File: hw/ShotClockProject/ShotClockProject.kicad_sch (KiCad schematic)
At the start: 8 parts, among them SW1 TK-6580S-1

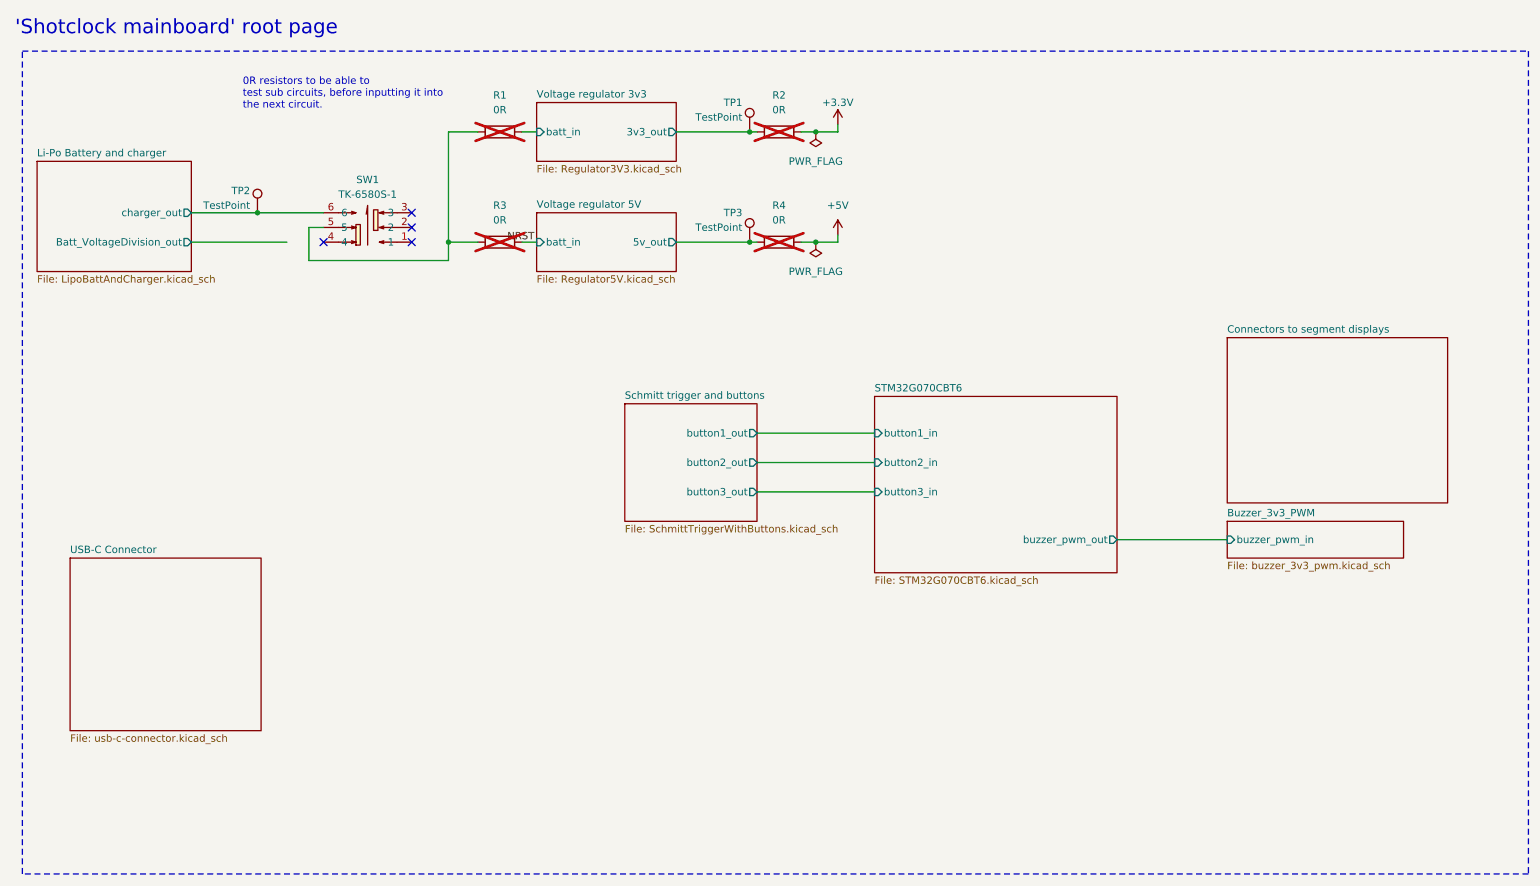
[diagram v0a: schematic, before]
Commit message: Routing on mainboard for LiPo charger
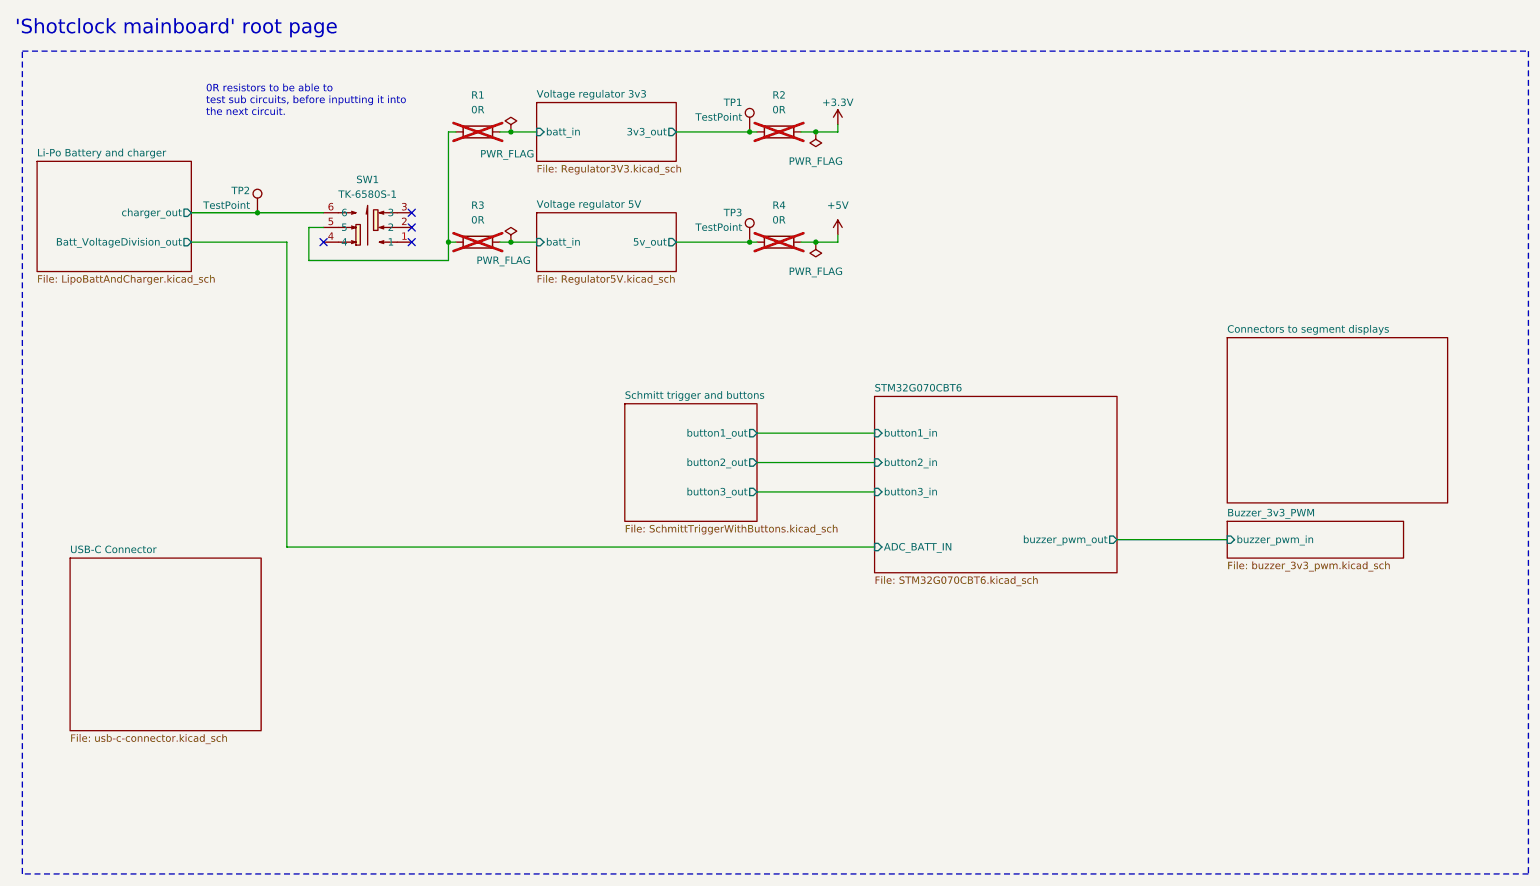
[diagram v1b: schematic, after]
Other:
- sheet STM32G070CBT6 ports: added ADC_BATT_IN; removed none
- moved on the sheet: R1, R3
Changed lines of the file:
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@@
   (junction (at 156.21 54.61) (diameter 0) (color 0 0 0 0)
+  )
+  (junction (at 103.505 54.61) (diameter 0) (color 0 0 0 0)
+  )
+  (junction (at 103.505 35.56) (diameter 0) (color 0 0 0 0)
   )
   (junction (at 59.69 49.53) (diameter 0) (color 0 0 0 0)
@@
     (stroke (width 0) (type default))
   )
+  (wire (pts (xy 103.505 54.61) (xy 107.95 54.61))
+    (stroke (width 0) (type default))
+  )
+  (wire (pts (xy 68.58 57.785) (xy 92.71 57.785))
+    (stroke (width 0) (type default))
+  )
   (wire (pts (xy 208.28 106.045) (xy 227.33 106.045))
     (stroke (width 0) (type default))
@@
     (stroke (width 0) (type default))
   )
+  (wire (pts (xy 92.71 35.56) (xy 92.71 54.61))
+    (stroke (width 0) (type default))
+  )
   (wire (pts (xy 156.21 54.61) (xy 160.02 54.61))
     (stroke (width 0) (type default))
   )
+  (wire (pts (xy 103.505 35.56) (xy 107.95 35.56))
+    (stroke (width 0) (type default))
+  )
   (wire (pts (xy 92.71 57.785) (xy 92.71 54.61))
     (stroke (width 0) (type default))
@@
     (stroke (width 0) (type default))
   )
-  (wire (pts (xy 105.41 35.56) (xy 107.95 35.56))
+  (wire (pts (xy 101.6 35.56) (xy 103.505 35.56))
     (stroke (width 0) (type default))
   )
@@
     (stroke (width 0) (type default))
   )
-  (wire (pts (xy 92.71 54.61) (xy 97.79 54.61))
+  (wire (pts (xy 92.71 54.61) (xy 93.98 54.61))
     (stroke (width 0) (type default))
   )
@@
     (stroke (width 0) (type default))
   )
-  (wire (pts (xy 92.71 35.56) (xy 92.71 54.61))
-    (stroke (width 0) (type default))
-  )
   (wire (pts (xy 160.02 54.61) (xy 160.02 53.34))
     (stroke (width 0) (type default))
   )
-  (wire (pts (xy 68.58 57.785) (xy 92.71 57.785))
-    (stroke (width 0) (type default))
-  )
-  (wire (pts (xy 97.79 35.56) (xy 92.71 35.56))
+  (wire (pts (xy 93.98 35.56) (xy 92.71 35.56))
     (stroke (width 0) (type default))
   )
@@
     (stroke (width 0) (type default))
   )
+  (wire (pts (xy 64.77 54.61) (xy 64.77 107.315))
+    (stroke (width 0) (type default))
+  )
   (wire (pts (xy 160.02 35.56) (xy 160.02 34.29))
     (stroke (width 0) (type default))
@@
     (stroke (width 0) (type default))
   )
-  (wire (pts (xy 105.41 54.61) (xy 107.95 54.61))
+  (wire (pts (xy 101.6 54.61) (xy 103.505 54.61))
     (stroke (width 0) (type default))
   )
   (wire (pts (xy 146.05 97.79) (xy 166.37 97.79))
+    (stroke (width 0) (type default))
+  )
+  (wire (pts (xy 64.77 107.315) (xy 166.37 107.315))
     (stroke (width 0) (type default))
   )
@@
   )
   (text "0R resistors to be able to \ntest sub circuits, before inputting it into\nthe next circuit."
-    (at 57.15 31.75 0)
+    (at 50.8 33.02 0)
     (effects (font (size 1.27 1.27)) (justify left bottom))
   )
   (text "'Shotclock mainboard' root page" (at 17.78 19.05 0)
     (effects (font (size 2.5 2.5) (color 255 0 0 1)) (justify left bottom))
-  )
-  (label "NRST" (at 102.87 54.61 0) (fields_autoplaced)
-    (effects (font (size 1.27 1.27)) (justify left bottom))
   )
   (symbol (lib_id "TK-6580S-1:TK-6580S-1") (at 78.74 52.07 90) (unit 1)
@@
     )
   )
-  (symbol (lib_id "Device:R") (at 101.6 35.56 90) (unit 1)
+  (symbol (lib_id "Device:R") (at 97.79 35.56 90) (unit 1)
     (in_bom yes) (on_board yes) (dnp yes) (fields_autoplaced)
-    (property "Reference" "R1" (at 101.6 29.21 90)
-      (effects (font (size 1.27 1.27)))
-    )
-    (property "Value" "0R" (at 101.6 31.75 90)
-      (effects (font (size 1.27 1.27)))
-    )
-    (property "Footprint" "Resistor_SMD:R_0402_1005Metric" (at 101.6 37.338 90)
-      (effects (font (size 1.27 1.27)) hide)
-    )
-    (property "Datasheet" "~" (at 101.6 35.56 0)
-      (effects (font (size 1.27 1.27)) hide)
-    )
-    (property "LCSC Part #" "C17168" (at 101.6 35.56 0)
-      (effects (font (size 1.27 1.27)) hide)
-    )
-    (property "LCSC Part" "C17168" (at 101.6 35.56 0)
+    (property "Reference" "R1" (at 97.79 29.21 90)
+      (effects (font (size 1.27 1.27)))
+    )
+    (property "Value" "0R" (at 97.79 31.75 90)
+      (effects (font (size 1.27 1.27)))
+    )
+    (property "Footprint" "Resistor_SMD:R_0402_1005Metric" (at 97.79 37.338 90)
+      (effects (font (size 1.27 1.27)) hide)
+    )
+    (property "Datasheet" "~" (at 97.79 35.56 0)
+      (effects (font (size 1.27 1.27)) hide)
+    )
+    (property "LCSC Part #" "C17168" (at 97.79 35.56 0)
+      (effects (font (size 1.27 1.27)) hide)
+    )
+    (property "LCSC Part" "C17168" (at 97.79 35.56 0)
       (effects (font (size 1.27 1.27)) hide)
     )
@@
     )
   )
+  (symbol (lib_id "power:PWR_FLAG") (at 103.505 35.56 0) (unit 1)
+    (in_bom yes) (on_board yes) (dnp no)
+    (property "Reference" "#FLG03" (at 103.505 33.655 0)
+      (effects (font (size 1.27 1.27)) hide)
+    )
+    (property "Value" "PWR_FLAG" (at 102.87 39.37 0)
+      (effects (font (size 1.27 1.27)))
+    )
+    (property "Footprint" "" (at 103.505 35.56 0)
+      (effects (font (size 1.27 1.27)) hide)
+    )
+    (property "Datasheet" "~" (at 103.505 35.56 0)
+      (effects (font (size 1.27 1.27)) hide)
+    )
+    (pin "1")
+    (instances
+      (project "ShotClockProject"
+        (path "/5fd859aa-754d-49c2-9762-3f7ebe3bb64c/d287d155-1951-4d4f-8d6c-570f03bc79f5"
+          (reference "#FLG03") (unit 1)
+        )
+        (path "/5fd859aa-754d-49c2-9762-3f7ebe3bb64c/17367eb9-0f4d-4017-b1ca-d50430410a5d"
+          (reference "#FLG08") (unit 1)
+        )
+        (path "/5fd859aa-754d-49c2-9762-3f7ebe3bb64c"
+          (reference "#FLG09") (unit 1)
+        )
+      )
+    )
+  )
+  (symbol (lib_id "power:PWR_FLAG") (at 103.505 54.61 0) (unit 1)
+    (in_bom yes) (on_board yes) (dnp no)
+    (property "Reference" "#FLG03" (at 103.505 52.705 0)
+      (effects (font (size 1.27 1.27)) hide)
+    )
+    (property "Value" "PWR_FLAG" (at 102.235 57.785 0)
+      (effects (font (size 1.27 1.27)))
+    )
+    (property "Footprint" "" (at 103.505 54.61 0)
+      (effects (font (size 1.27 1.27)) hide)
+    )
+    (property "Datasheet" "~" (at 103.505 54.61 0)
+      (effects (font (size 1.27 1.27)) hide)
+    )
+    (pin "1")
+    (instances
+      (project "ShotClockProject"
+        (path "/5fd859aa-754d-49c2-9762-3f7ebe3bb64c/d287d155-1951-4d4f-8d6c-570f03bc79f5"
+          (reference "#FLG03") (unit 1)
+        )
+        (path "/5fd859aa-754d-49c2-9762-3f7ebe3bb64c/17367eb9-0f4d-4017-b1ca-d50430410a5d"
+          (reference "#FLG08") (unit 1)
+        )
+        (path "/5fd859aa-754d-49c2-9762-3f7ebe3bb64c"
+          (reference "#FLG07") (unit 1)
+        )
+      )
+    )
+  )
   (symbol (lib_id "power:PWR_FLAG") (at 156.21 35.56 180) (unit 1)
     (in_bom yes) (on_board yes) (dnp no) (fields_autoplaced)
@@
     )
   )
-  (symbol (lib_id "Device:R") (at 101.6 54.61 90) (unit 1)
+  (symbol (lib_id "Device:R") (at 97.79 54.61 90) (unit 1)
     (in_bom yes) (on_board yes) (dnp yes) (fields_autoplaced)
-    (property "Reference" "R3" (at 101.6 48.26 90)
-      (effects (font (size 1.27 1.27)))
-    )
-    (property "Value" "0R" (at 101.6 50.8 90)
-      (effects (font (size 1.27 1.27)))
-    )
-    (property "Footprint" "Resistor_SMD:R_0402_1005Metric" (at 101.6 56.388 90)
-      (effects (font (size 1.27 1.27)) hide)
-    )
-    (property "Datasheet" "~" (at 101.6 54.61 0)
-      (effects (font (size 1.27 1.27)) hide)
-    )
-    (property "LCSC Part #" "C17168" (at 101.6 54.61 0)
-      (effects (font (size 1.27 1.27)) hide)
-    )
-    (property "LCSC Part" "C17168" (at 101.6 54.61 0)
+    (property "Reference" "R3" (at 97.79 48.26 90)
+      (effects (font (size 1.27 1.27)))
+    )
+    (property "Value" "0R" (at 97.79 50.8 90)
+      (effects (font (size 1.27 1.27)))
+    )
+    (property "Footprint" "Resistor_SMD:R_0402_1005Metric" (at 97.79 56.388 90)
+      (effects (font (size 1.27 1.27)) hide)
+    )
+    (property "Datasheet" "~" (at 97.79 54.61 0)
+      (effects (font (size 1.27 1.27)) hide)
+    )
+    (property "LCSC Part #" "C17168" (at 97.79 54.61 0)
+      (effects (font (size 1.27 1.27)) hide)
+    )
+    (property "LCSC Part" "C17168" (at 97.79 54.61 0)
       (effects (font (size 1.27 1.27)) hide)
     )
@@
       (effects (font (size 1.27 1.27)) (justify right))
     )
-    (instances
+    (pin "ADC_BATT_IN" input (at 166.37 107.315 180)
+      (effects (font (size 1.27 1.27)) (justify left))
+    )
+    (instances

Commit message: Finished mainboard routing
Reconfigered pins to make routing easier/cleaner
Placed copper fills as much as possible to create an even plating index
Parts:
- removed TP1, TP3: TestPoint, TestPoint:TestPoint_Pad_D1.0mm, symbol Connector:TestPoint
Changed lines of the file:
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@@
     (comment 1 "Author: M. de Waard")
-  )
-  (junction (at 144.78 54.61) (diameter 0) (color 0 0 0 0)
   )
   (junction (at 92.71 54.61) (diameter 0) (color 0 0 0 0)
@@
   )
   (junction (at 156.21 35.56) (diameter 0) (color 0 0 0 0)
-  )
-  (junction (at 144.78 35.56) (diameter 0) (color 0 0 0 0)
   )
   (no_connect (at 86.36 54.61))
@@
     (stroke (width 0) (type default))
   )
-  (wire (pts (xy 132.08 54.61) (xy 144.78 54.61))
-    (stroke (width 0) (type default))
-  )
   (wire (pts (xy 92.71 35.56) (xy 92.71 54.61))
     (stroke (width 0) (type default))
@@
     (stroke (width 0) (type default))
   )
-  (wire (pts (xy 144.78 35.56) (xy 146.05 35.56))
+  (wire (pts (xy 132.08 35.56) (xy 146.05 35.56))
     (stroke (width 0) (type default))
   )
@@
     (stroke (width 0) (type default))
   )
-  (wire (pts (xy 144.78 54.61) (xy 146.05 54.61))
+  (wire (pts (xy 132.08 54.61) (xy 146.05 54.61))
     (stroke (width 0) (type default))
   )
@@
   )
   (wire (pts (xy 93.98 35.56) (xy 92.71 35.56))
-    (stroke (width 0) (type default))
-  )
-  (wire (pts (xy 132.08 35.56) (xy 144.78 35.56))
     (stroke (width 0) (type default))
   )
@@
     )
   )
-  (symbol (lib_id "Connector:TestPoint") (at 144.78 54.61 0) (mirror y) (unit 1)
-    (in_bom yes) (on_board yes) (dnp no)
-    (property "Reference" "TP3" (at 143.51 49.53 0)
-      (effects (font (size 1.27 1.27)) (justify left))
-    )
-    (property "Value" "TestPoint" (at 143.51 52.07 0)
-      (effects (font (size 1.27 1.27)) (justify left))
-    )
-    (property "Footprint" "TestPoint:TestPoint_Pad_D1.0mm" (at 139.7 54.61 0)
-      (effects (font (size 1.27 1.27)) hide)
-    )
-    (property "Datasheet" "~" (at 139.7 54.61 0)
-      (effects (font (size 1.27 1.27)) hide)
-    )
-    (property "LCSC Part #" "" (at 144.78 54.61 0)
-      (effects (font (size 1.27 1.27)) hide)
-    )
-    (property "LCSC Part" "" (at 144.78 54.61 0)
-      (effects (font (size 1.27 1.27)) hide)
-    )
-    (pin "1")
-    (instances
-      (project "ShotClockProject"
-        (path "/5fd859aa-754d-49c2-9762-3f7ebe3bb64c"
-          (reference "TP3") (unit 1)
-        )
-        (path "/5fd859aa-754d-49c2-9762-3f7ebe3bb64c/17367eb9-0f4d-4017-b1ca-d50430410a5d"
-          (reference "TP8") (unit 1)
-        )
-      )
-    )
-  )
   (symbol (lib_id "power:PWR_FLAG") (at 156.21 54.61 180) (unit 1)
     (in_bom yes) (on_board yes) (dnp no) (fields_autoplaced)
@@
         )
       )
-    )
-  )
-  (symbol (lib_id "Connector:TestPoint") (at 144.78 35.56 0) (mirror y) (unit 1)
-    (in_bom yes) (on_board yes) (dnp no)
-    (property "Reference" "TP1" (at 143.51 30.48 0)
-      (effects (font (size 1.27 1.27)) (justify left))
-    )
-    (property "Value" "TestPoint" (at 143.51 33.02 0)
-      (effects (font (size 1.27 1.27)) (justify left))
-    )
-    (property "Footprint" "TestPoint:TestPoint_Pad_D1.0mm" (at 139.7 35.56 0)
-      (effects (font (size 1.27 1.27)) hide)
-    )
-    (property "Datasheet" "~" (at 139.7 35.56 0)
-      (effects (font (size 1.27 1.27)) hide)
-    )
-    (property "LCSC Part #" "" (at 144.78 35.56 0)
-      (effects (font (size 1.27 1.27)) hide)
-    )
-    (property "LCSC Part" "" (at 144.78 35.56 0)
-      (effects (font (size 1.27 1.27)) hide)
-    )
-    (pin "1")
-    (instances
-      (project "ShotClockProject"
-        (path "/5fd859aa-754d-49c2-9762-3f7ebe3bb64c"
-          (reference "TP1") (unit 1)
-        )
-        (path "/5fd859aa-754d-49c2-9762-3f7ebe3bb64c/17367eb9-0f4d-4017-b1ca-d50430410a5d"
-          (reference "TP8") (unit 1)
-        )
-      )

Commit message: Finished routing and added silk + part nmbr
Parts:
- R1, R2, R3, R4: LCSC Part # C17168 -> (none)
- SW1: LCSC Part # C528774 -> (none)
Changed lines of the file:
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@@
       (effects (font (size 1.27 1.27)) hide)
     )
-    (property "LCSC Part #" "C528774" (at 78.74 52.07 0)
+    (property "LCSC Part #" "" (at 78.74 52.07 0)
       (effects (font (size 1.27 1.27)) hide)
     )
@@
       (effects (font (size 1.27 1.27)) hide)
     )
-    (property "LCSC Part #" "C17168" (at 149.86 35.56 0)
+    (property "LCSC Part #" "" (at 149.86 35.56 0)
       (effects (font (size 1.27 1.27)) hide)
     )
@@
       (effects (font (size 1.27 1.27)) hide)
     )
-    (property "LCSC Part #" "C17168" (at 97.79 35.56 0)
+    (property "LCSC Part #" "" (at 97.79 35.56 0)
       (effects (font (size 1.27 1.27)) hide)
     )
@@
       (effects (font (size 1.27 1.27)) hide)
     )
-    (property "LCSC Part #" "C17168" (at 149.86 54.61 0)
+    (property "LCSC Part #" "" (at 149.86 54.61 0)
       (effects (font (size 1.27 1.27)) hide)
     )
@@
       (effects (font (size 1.27 1.27)) hide)
     )
-    (property "LCSC Part #" "C17168" (at 97.79 54.61 0)
-      (effects (font (size 1.27 1.27)) hide)
-    )
+    (property "LCSC Part #" "" (at 97.79 54.61 0)
+      (effects (font (size 1.27 1.27)) hide)
+    )
